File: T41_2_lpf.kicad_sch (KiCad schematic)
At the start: 41 parts, among them J1 5-1814832-1, J2 5-1814832-1, J3 5-1814832-1, J4 Conn_02x08_Odd_Even, J5 Conn_02x05_Odd_Even, J6 B2B-XH-A_LF__SN_, Q6 Q_NMOS_GSD, U12 4002, U13 TCA9534

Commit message: Commit just prior to pushing to Github.  Design not complete.
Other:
- note added: "12V_FIL not used???"

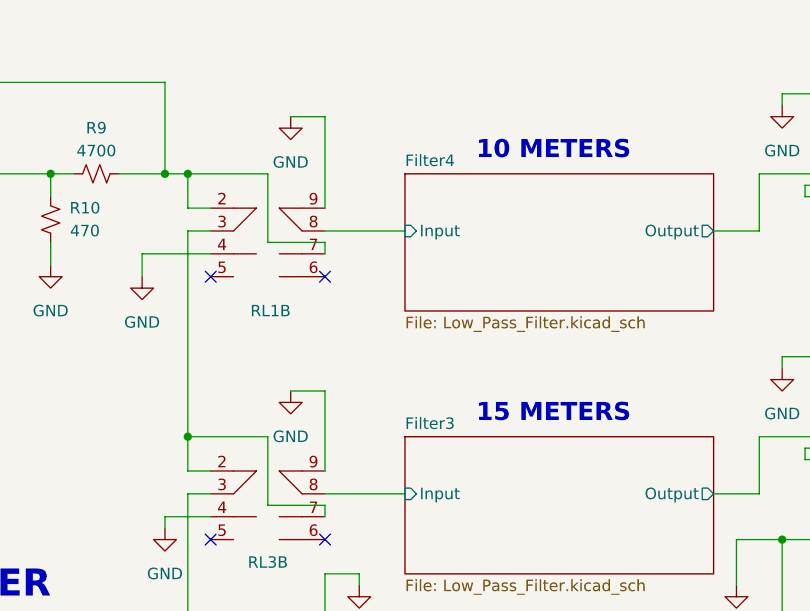
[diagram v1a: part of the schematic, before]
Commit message: Trying to improve schematic by adding capacitor values to all bands.
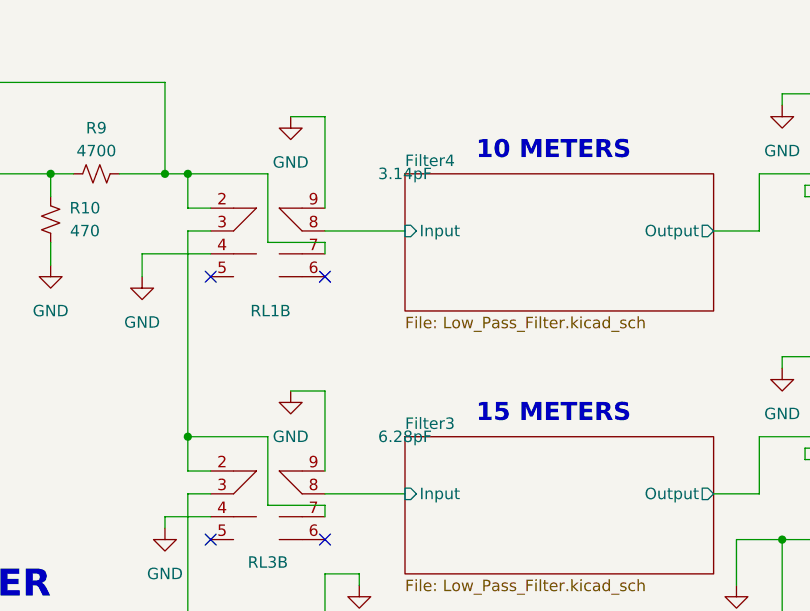
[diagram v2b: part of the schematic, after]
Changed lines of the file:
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@@
+			)
+		)
+		(property "C_1" "3.14pF"
+			(at 172.72 25.4 0)
+			(effects
+				(font
+					(size 1.27 1.27)
+				)
 			)
 		)
@@
 			)
 		)
+		(property "C_1" "6.28pF"
+			(at 172.72 54.61 0)
+			(effects
+				(font
+					(size 1.27 1.27)
+				)
+			)
+		)

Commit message: T41-2 LPF V1.4 to fab.
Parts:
- removed C2: 0.1uF, Capacitor_SMD:C_1206_3216Metric, symbol Device:C_Small
- removed FB12: 28F0121-0SR-10, Inductor_SMD:L_1206_3216Metric, symbol LairdFerrBead:28F0121-0SR-10
- removed R10: 470, Resistor_SMD:R_1206_3216Metric, symbol Device:R_Small_US
- removed R7, R8: 0, Resistor_SMD:R_1206_3216Metric, symbol Device:R_Small_US
- removed R9: 4700, Resistor_SMD:R_1206_3216Metric, symbol Device:R_Small_US
- added TP1: TestPoint, Connector_PinHeader_2.54mm:PinHeader_1x01_P2.54mm_Vertical, symbol Connector:TestPoint
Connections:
- net 12VIN is gone; now on net 12V_IN: J4.5 (Pin_5), J4.6 (Pin_6)
- net 3_3V is gone; now on net 3_3V_IN: FB13.1, J4.13 (Pin_13), J4.14 (Pin_14)
- net GND: now also TP1.1
- no-connect marks 37 -> 38
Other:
- note added: "#26 AWG"
- note added: "25 TURNS"
- note added: "T68-2"
- note added: "TO POWER AMPLIFIER"
- note added: "This is a grounded header pin for attaching a probe."
- note removed: "12V_FIL not used???"
- note removed: "FROM POWER AMPLIFIER"
- note removed: "POWER AMPLIFIER"

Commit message: Work in progress just prior to publish.
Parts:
- RL1, RL10, RL11, RL2, RL3, RL4, RL5, RL6, RL7, RL8, RL9: value ~ -> (none)
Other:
- note added: "16T 13T 16T"
- note added: "PANASONIC RELAYS"
- note added: "T37-6 TOROIDS"
- note added: "T44-2 TOROIDS"

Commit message: Ready to fab version 1.5
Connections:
- net Filter/Input renamed Filter5/Input
- net Filter/Output renamed Filter5/Output
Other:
- removed sheet Filter
- added sheet Filter5 (Low_Pass_Filter_80M.kicad_sch)
- note removed: "16T 13T 16T"
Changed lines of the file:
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@@
 		(rev "V1.4")
 	)
-	(text "16T 13T 16T"
-		(exclude_from_sim no)
-		(at 188.468 149.86 0)
-		(effects
-			(font
-				(size 1.5 1.5)
-				(thickness 0.254)
-				(bold yes)
-			)
-		)
-	)
 	(text "TO RECEIVER"
 		(exclude_from_sim no)
@@
 	(text "T44-2 TOROIDS"
 		(exclude_from_sim no)
-		(at 188.468 146.812 0)
+		(at 188.976 141.478 0)
 		(effects
 			(font
@@
 			(color 0 0 0 0)
 		)
-		(property "Sheetname" "Filter"
+		(property "Sheetname" "Filter5"
 			(at 172.72 136.4484 0)
 			(show_name no)
@@
 			)
 		)
-		(property "Sheetfile" "Low_Pass_Filter.kicad_sch"
+		(property "Sheetfile" "Low_Pass_Filter_80M.kicad_sch"
 			(at 172.72 152.9846 0)
 			(show_name no)
@@
 			(project "T41_2_lpf"
 				(path "/5fc700c6-272f-41b7-8650-23a96fb06ce8"
-					(page "3")
+					(page "8")
 				)
 			)
